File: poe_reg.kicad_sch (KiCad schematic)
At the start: 34 parts, among them Q11 BSS138W, T2 POE30P-50L, U5 MP6004GQ-Z

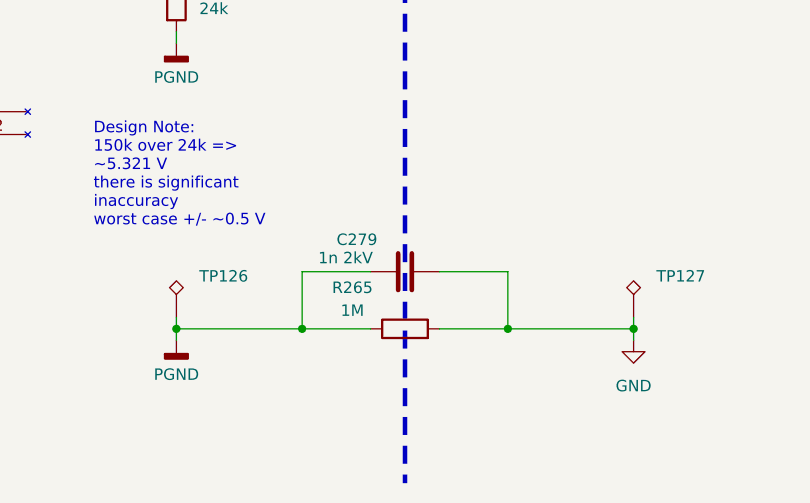
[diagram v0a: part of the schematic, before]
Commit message: fixed some more schematic review
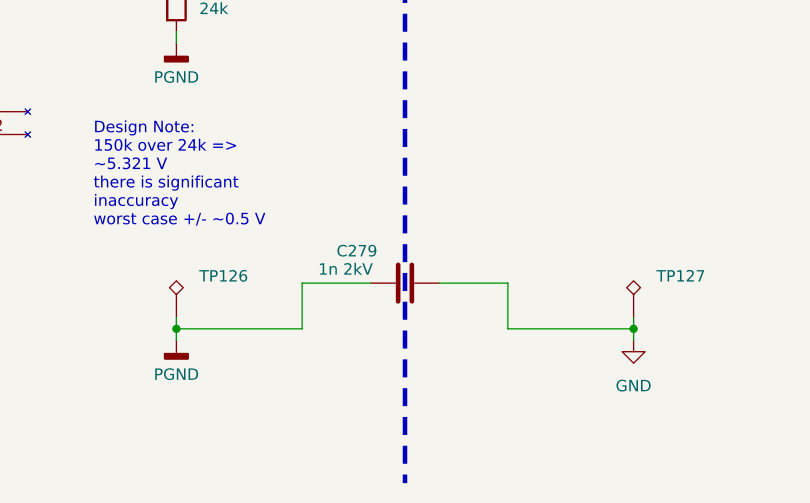
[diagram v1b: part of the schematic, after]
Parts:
- removed R265: 1M, Resistor_SMD:R_1206_3216Metric, symbol Device:R
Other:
- moved on the sheet: C279

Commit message: did some review cleanup
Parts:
- R104: footprint Resistor_SMD:R_0603_1608Metric -> Resistor_SMD:R_0402_1005Metric
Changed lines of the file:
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@@
 			)
 		)
-		(property "Footprint" "Resistor_SMD:R_0603_1608Metric"
+		(property "Footprint" "Resistor_SMD:R_0402_1005Metric"
 			(at 94.742 171.45 90)
 			(hide yes)
